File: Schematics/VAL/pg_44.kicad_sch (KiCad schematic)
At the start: 14 parts

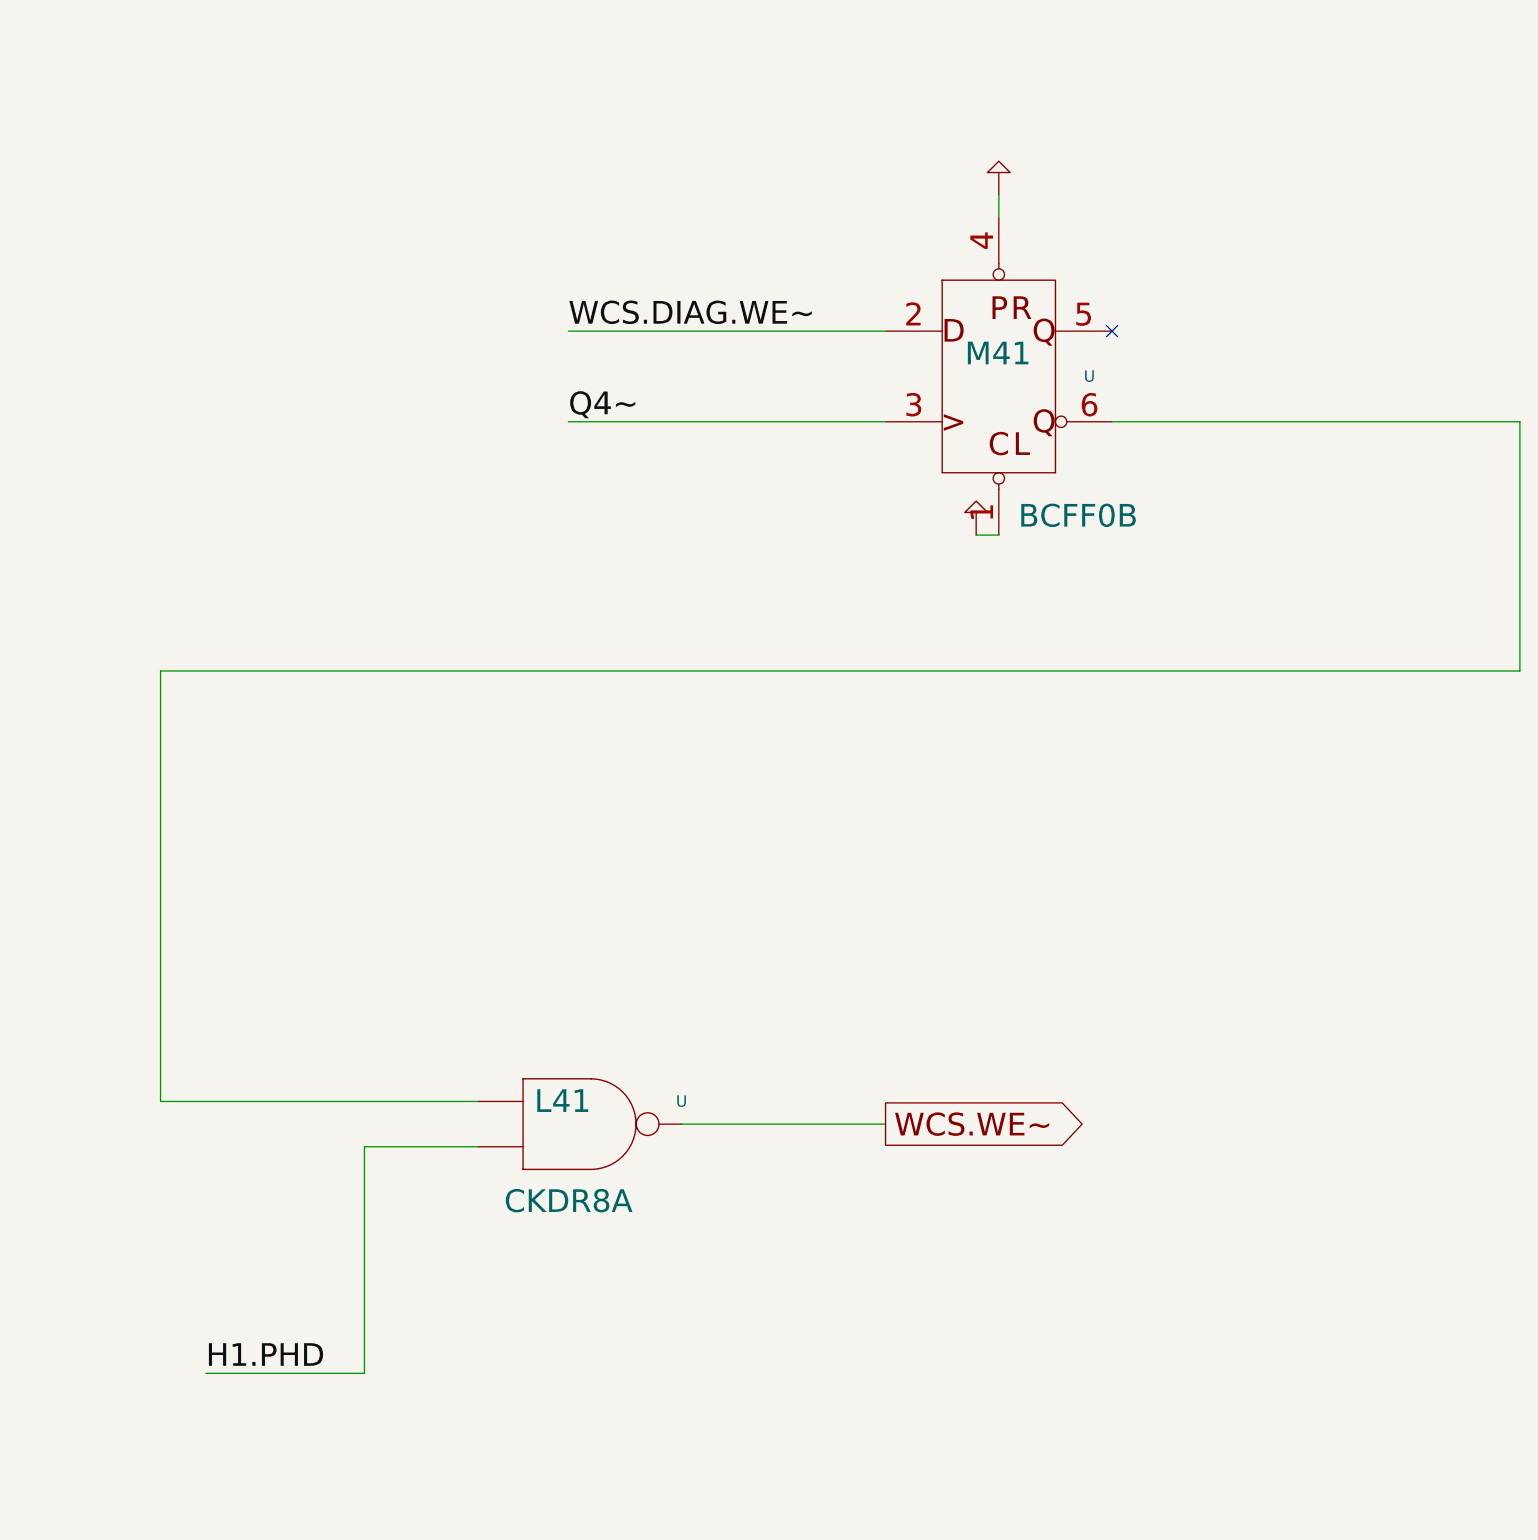
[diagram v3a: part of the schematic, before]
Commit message: Clean up UADR path
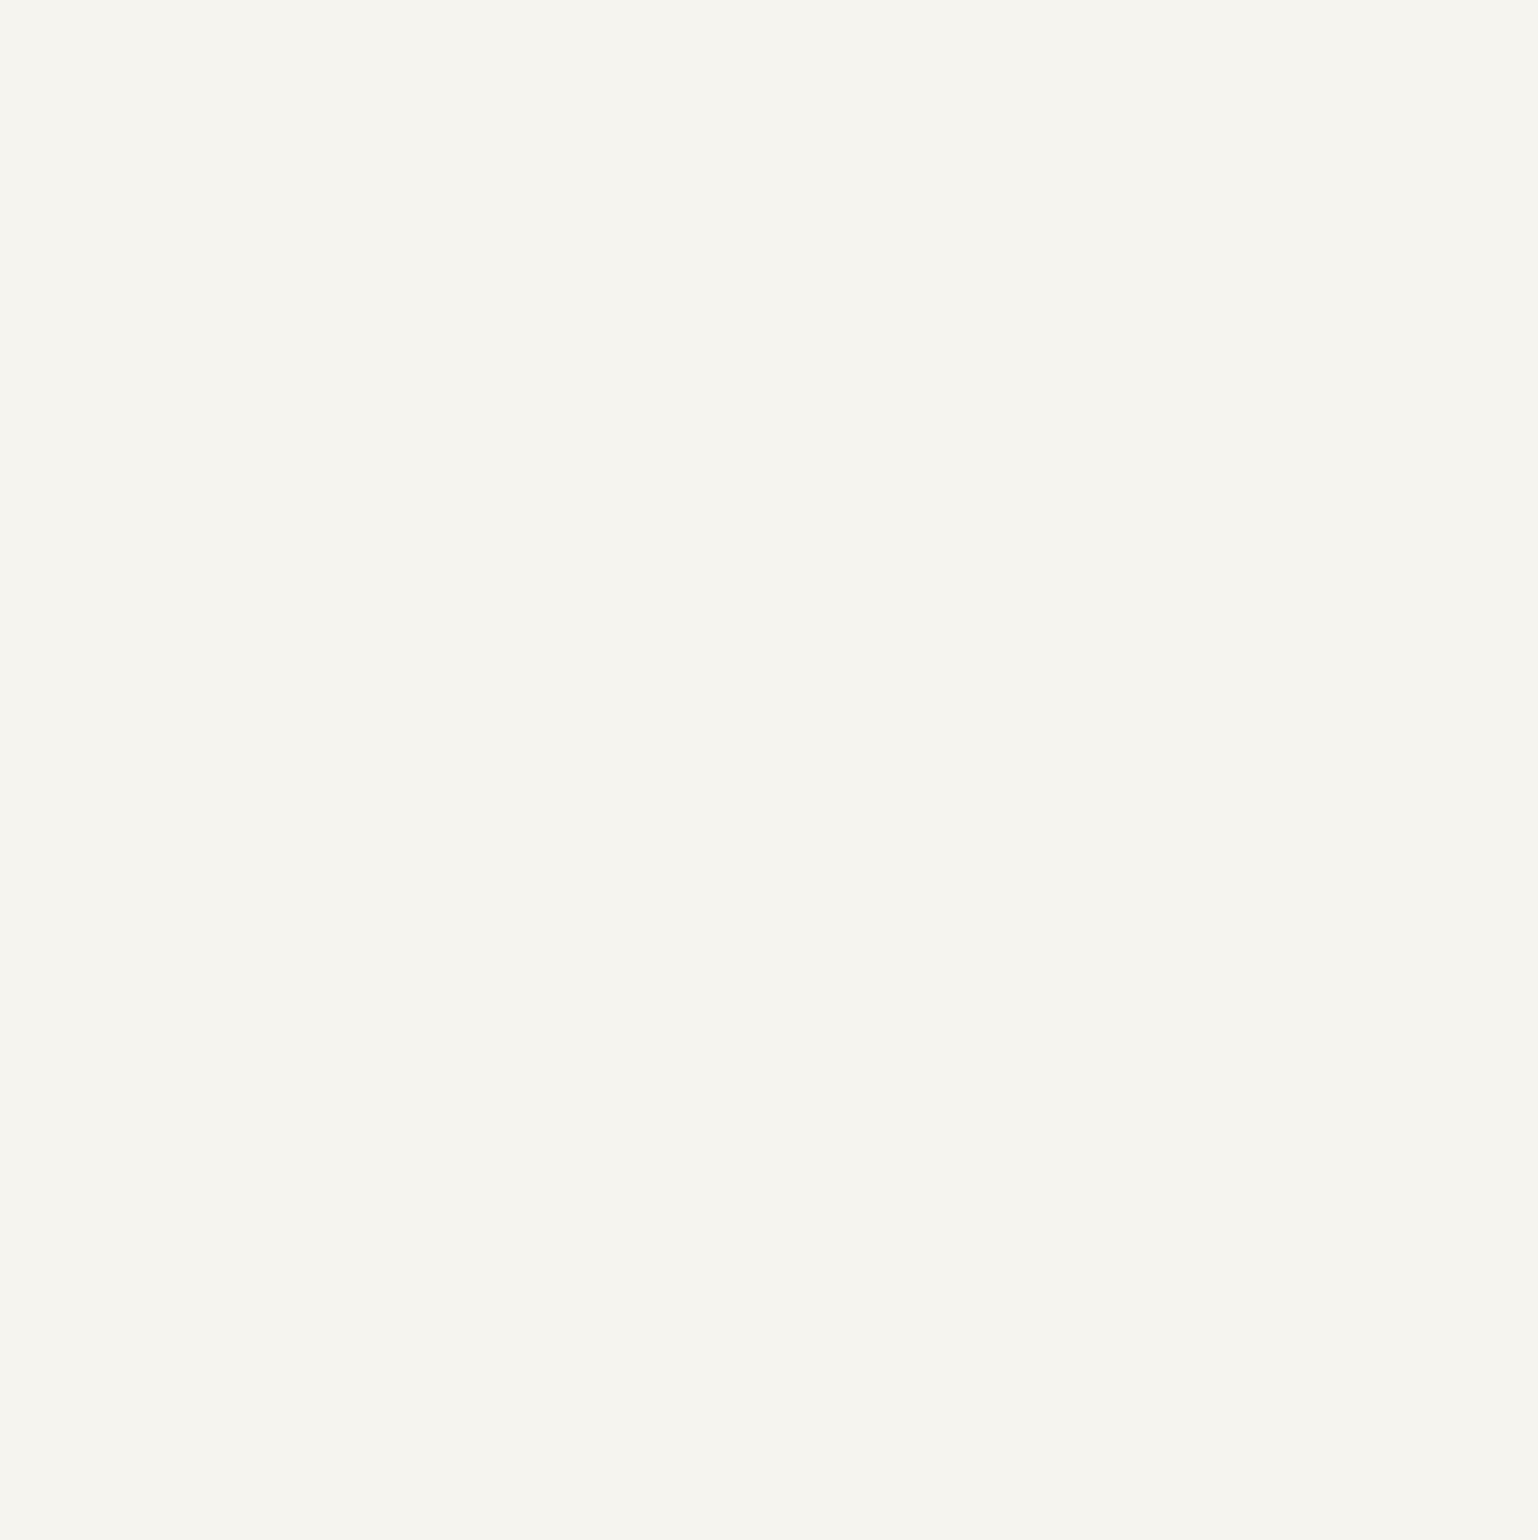
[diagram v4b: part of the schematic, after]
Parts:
- removed U: (no value), symbol r1000:F74
- removed U: (no value), symbol r1000:F37
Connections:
- no-connect marks 16 -> 15
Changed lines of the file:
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@@
   (no_connect (at 223.52 287.02))
   (no_connect (at 279.4 154.94))
-  (no_connect (at 528.32 132.08))
   (no_connect (at 223.52 281.94))
   (no_connect (at 279.4 124.46))
@@
     (stroke (width 0) (type default))
   )
-  (wire (pts (xy 444.5 223.52) (xy 444.5 248.92))
-    (stroke (width 0) (type default))
-  )
   (wire (pts (xy 60.96 22.86) (xy 78.74 22.86))
     (stroke (width 0) (type default))
   )
-  (wire (pts (xy 467.36 132.08) (xy 502.92 132.08))
-    (stroke (width 0) (type default))
-  )
   (wire (pts (xy 279.4 129.54) (xy 274.32 129.54))
     (stroke (width 0) (type default))
@@
     (stroke (width 0) (type default))
   )
-  (wire (pts (xy 528.32 142.24) (xy 574.04 142.24))
-    (stroke (width 0) (type default))
-  )
   (wire (pts (xy 231.14 91.44) (xy 231.14 114.3))
     (stroke (width 0) (type default))
@@
     (stroke (width 0) (type default))
   )
-  (wire (pts (xy 467.36 142.24) (xy 502.92 142.24))
-    (stroke (width 0) (type default))
-  )
   (wire (pts (xy 60.96 33.02) (xy 78.74 33.02))
     (stroke (width 0) (type default))
@@
     (stroke (width 0) (type default))
   )
-  (wire (pts (xy 421.64 170.18) (xy 421.64 218.44))
-    (stroke (width 0) (type default))
-  )
   (wire (pts (xy 172.72 40.64) (xy 182.88 40.64))
     (stroke (width 0) (type default))
@@
     (stroke (width 0) (type default))
   )
-  (wire (pts (xy 513.08 154.94) (xy 515.62 154.94))
-    (stroke (width 0) (type default))
-  )
   (wire (pts (xy 246.38 48.26) (xy 269.24 48.26))
     (stroke (width 0) (type default))
   )
-  (wire (pts (xy 421.64 218.44) (xy 457.2 218.44))
-    (stroke (width 0) (type default))
-  )
-  (wire (pts (xy 457.2 223.52) (xy 444.5 223.52))
-    (stroke (width 0) (type default))
-  )
   (wire (pts (xy 193.04 180.34) (xy 198.12 180.34))
     (stroke (width 0) (type default))
@@
     (stroke (width 0) (type default))
   )
-  (wire (pts (xy 426.72 248.92) (xy 444.5 248.92))
-    (stroke (width 0) (type default))
-  )
   (wire (pts (xy 231.14 165.1) (xy 279.4 165.1))
     (stroke (width 0) (type default))
@@
     (stroke (width 0) (type default))
   )
-  (wire (pts (xy 574.04 170.18) (xy 421.64 170.18))
-    (stroke (width 0) (type default))
-  )
   (wire (pts (xy 302.26 121.92) (xy 309.88 121.92))
     (stroke (width 0) (type default))
   )
-  (wire (pts (xy 515.62 116.84) (xy 515.62 119.38))
-    (stroke (width 0) (type default))
-  )
-  (wire (pts (xy 574.04 142.24) (xy 574.04 170.18))
-    (stroke (width 0) (type default))
-  )
   (wire (pts (xy 220.98 22.86) (xy 269.24 22.86))
     (stroke (width 0) (type default))
@@
     (stroke (width 0) (type default))
   )
-  (wire (pts (xy 480.06 220.98) (xy 502.92 220.98))
-    (stroke (width 0) (type default))
-  )
   (wire (pts (xy 292.1 30.48) (xy 299.72 30.48))
     (stroke (width 0) (type default))
@@
     (effects (font (size 2.54 2.54)) (justify left bottom))
   )
-  (label "WCS.DIAG.WE~" (at 467.36 132.08 0) (fields_autoplaced)
-    (effects (font (size 2.54 2.54)) (justify left bottom))
-  )
-  (label "H1.PHD" (at 426.72 248.92 0) (fields_autoplaced)
-    (effects (font (size 2.54 2.54)) (justify left bottom))
-  )
   (label "H2E" (at 160.02 91.44 0) (fields_autoplaced)
     (effects (font (size 2.54 2.54)) (justify left bottom))
@@
   )
   (label "CLK.2XE" (at 160.02 127 0) (fields_autoplaced)
-    (effects (font (size 2.54 2.54)) (justify left bottom))
-  )
-  (label "Q4~" (at 467.36 142.24 0) (fields_autoplaced)
     (effects (font (size 2.54 2.54)) (justify left bottom))
   )
@@
     )
   )
-  (global_label "WCS.WE~" (shape output) (at 502.92 220.98 0) (fields_autoplaced)
-    (effects (font (size 2.54 2.54)) (justify left))
-    (property "Intersheet References" "${INTERSHEET_REFS}" (id 0) (at 526.2517 220.8213 0)
-      (effects (font (size 1.905 1.905)) (justify left))
-    )
-  )
   (global_label "RAM_STOP~" (shape input) (at 259.08 40.64 180) (fields_autoplaced)
     (effects (font (size 2.54 2.54)) (justify right))
@@
       (effects (font (size 1.905 1.905)) (justify right))
     )
-  )
-  (symbol (lib_id "r1000:F74") (at 513.08 134.62 0) (unit 1)
-    (in_bom yes) (on_board yes)
-    (default_instance (reference "U") (unit 1) (value "") (footprint ""))
-    (property "Reference" "U" (id 0) (at 525.78 137.16 0)
-      (effects (font (size 1.27 1.27)))
-    )
-    (property "Value" "" (id 1) (at 511.81 139.7 0)
-      (effects (font (size 2.54 2.54)) (justify left))
-    )
-    (property "Footprint" "" (id 2) (at 514.35 135.89 0)
-      (effects (font (size 1.27 1.27)) hide)
-    )
-    (property "Datasheet" "" (id 3) (at 514.35 135.89 0)
-      (effects (font (size 1.27 1.27)) hide)
-    )
-    (property "Location" "M41" (id 4) (at 511.81 134.62 0)
-      (effects (font (size 2.54 2.54)) (justify left))
-    )
-    (property "Name" "BCFF0B" (id 5) (at 524.51 154.305 0)
-      (effects (font (size 2.54 2.54)) (justify bottom))
-    )
-    (pin "1")
-    (pin "2")
-    (pin "3")
-    (pin "4")
-    (pin "5")
-    (pin "6")
   )
   (symbol (lib_id "r1000:F40") (at 276.86 50.8 0) (unit 1)
@@
     (pin "9")
   )
-  (symbol (lib_id "r1000:PU") (at 513.08 154.94 0) (unit 1)
-    (in_bom yes) (on_board yes)
-    (default_instance (reference "U") (unit 1) (value "") (footprint ""))
-    (property "Reference" "U" (id 0) (at 513.08 154.94 0)
-      (effects (font (size 1.27 1.27)) hide)
-    )
-    (property "Value" "" (id 1) (at 513.08 154.94 0)
-      (effects (font (size 1.27 1.27)) hide)
-    )
-    (property "Footprint" "" (id 2) (at 513.08 154.94 0)
-      (effects (font (size 1.27 1.27)) hide)
-    )
-    (property "Datasheet" "" (id 3) (at 513.08 154.94 0)
-      (effects (font (size 1.27 1.27)) hide)
-    )
-    (pin "1")
-  )
   (symbol (lib_id "r1000:F40") (at 287.02 121.92 0) (unit 1)
     (in_bom yes) (on_board yes)
@@
     (pin "6")
   )
-  (symbol (lib_id "r1000:PU") (at 515.62 116.84 0) (unit 1)
-    (in_bom yes) (on_board yes)
-    (default_instance (reference "U") (unit 1) (value "") (footprint ""))
-    (property "Reference" "U" (id 0) (at 515.62 116.84 0)
-      (effects (font (size 1.27 1.27)) hide)
-    )
-    (property "Value" "" (id 1) (at 515.62 116.84 0)
-      (effects (font (size 1.27 1.27)) hide)
-    )
-    (property "Footprint" "" (id 2) (at 515.62 116.84 0)
-      (effects (font (size 1.27 1.27)) hide)
-    )
-    (property "Datasheet" "" (id 3) (at 515.62 116.84 0)
-      (effects (font (size 1.27 1.27)) hide)
-    )
-    (pin "1")
-  )
   (symbol (lib_id "r1000:F02") (at 205.74 55.88 0) (unit 1) (convert 2)
     (in_bom yes) (on_board yes)
@@
     (pin "6")
   )
-  (symbol (lib_id "r1000:F37") (at 464.82 218.44 0) (unit 1)
-    (in_bom yes) (on_board yes)
-    (default_instance (reference "U") (unit 1) (value "") (footprint ""))
-    (property "Reference" "U" (id 0) (at 480.06 218.44 0)
-      (effects (font (size 1.27 1.27)))
-    )
-    (property "Value" "" (id 1) (at 466.725 223.52 0)
-      (effects (font (size 2.54 2.54)))
-    )
-    (property "Footprint" "" (id 2) (at 464.82 205.74 0)
-      (effects (font (size 1.27 1.27)) hide)
-    )
-    (property "Datasheet" "" (id 3) (at 464.82 205.74 0)
-      (effects (font (size 1.27 1.27)) hide)
-    )
-    (property "Location" "L41" (id 4) (at 466.725 218.44 0)
-      (effects (font (size 2.54 2.54)))
-    )
-    (property "Name" "CKDR8A" (id 5) (at 467.36 231.14 0)
-      (effects (font (size 2.54 2.54)) (justify bottom))
-    )
-    (pin "1")
-    (pin "2")
-    (pin "3")
-  )
   (symbol (lib_id "r1000:PU") (at 210.82 238.76 0) (unit 1)

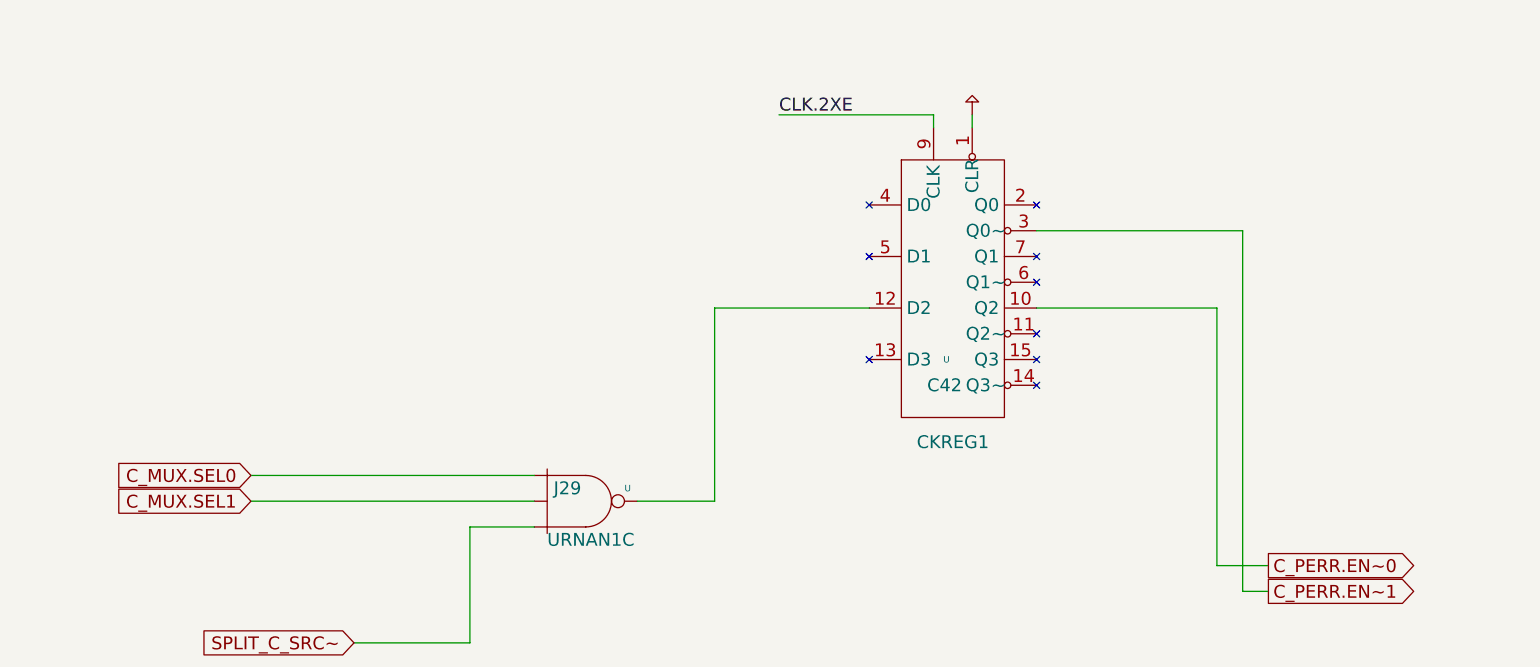
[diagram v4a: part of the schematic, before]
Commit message: Delete blank sheets
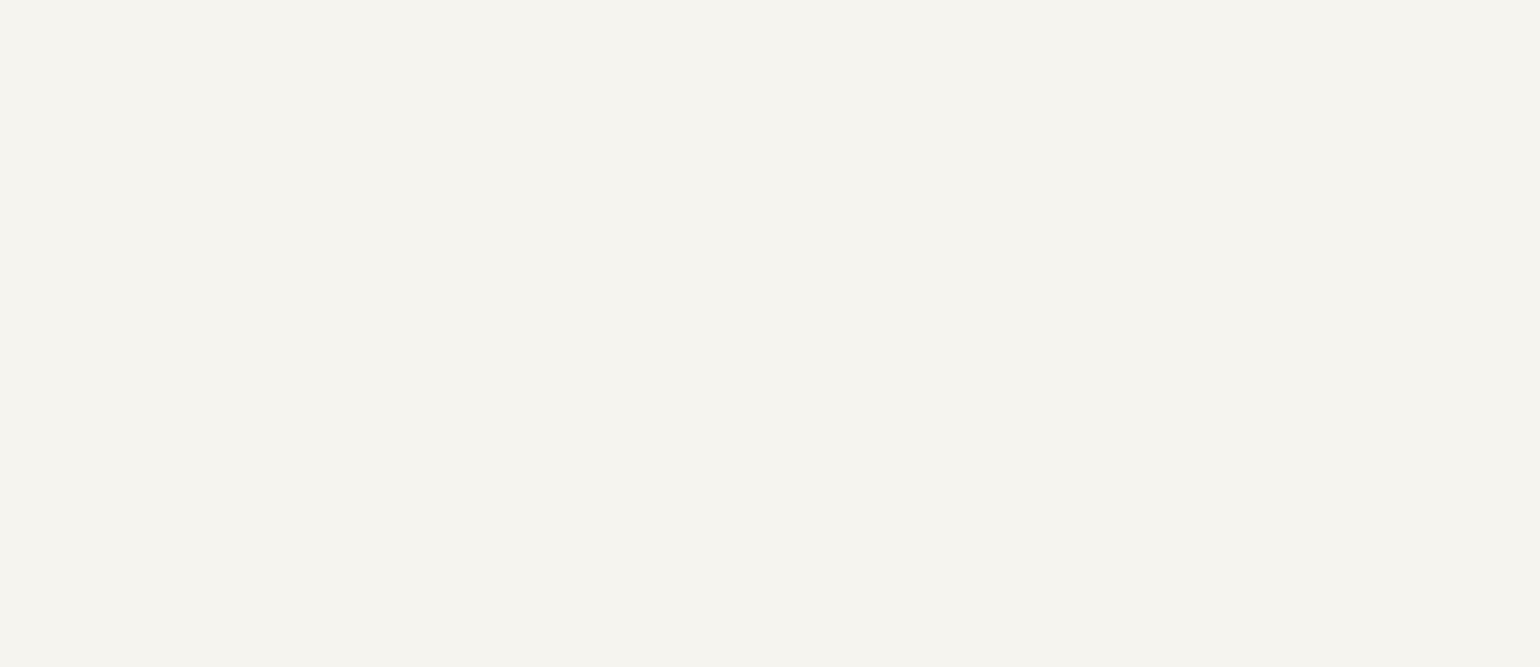
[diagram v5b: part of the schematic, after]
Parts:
- removed U: (no value), symbol r1000:F175
- removed U: (no value), symbol r1000:F10
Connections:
- no-connect marks 15 -> 6
